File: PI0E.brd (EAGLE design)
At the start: 36 parts, among them T1 WE-LAN-10/100/1000-BASE-T,749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, X1 22-23-2021, X2 22-23-2021

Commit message: fixed missing RX line
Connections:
- net 3: now also T1.1
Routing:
- net 3: track 0.00 -> 23.4 mm, vias 0 -> 2
- net 1: track 21.2 -> 23.2 mm
- net 2: track 19.6 -> 21.3 mm
- net 6: track 17.5 -> 19.1 mm
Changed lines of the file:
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@@
 <layer number="17" name="Pads" color="2" fill="1" visible="yes" active="yes"/>
 <layer number="18" name="Vias" color="2" fill="1" visible="yes" active="yes"/>
-<layer number="19" name="Unrouted" color="6" fill="1" visible="no" active="yes"/>
+<layer number="19" name="Unrouted" color="6" fill="1" visible="yes" active="yes"/>
 <layer number="20" name="Dimension" color="15" fill="1" visible="no" active="yes"/>
 <layer number="21" name="tPlace" color="7" fill="1" visible="yes" active="yes"/>
@@
 <contactref element="U$4" pad="2"/>
 <contactref element="T1" pad="8"/>
-<wire x1="66.01" y1="29.761" x2="68.283" y2="29.761" width="0.4064" layer="1"/>
-<wire x1="68.283" y1="29.761" x2="69.596" y2="28.448" width="0.4064" layer="1"/>
-<wire x1="69.596" y1="28.448" x2="69.596" y2="20.828" width="0.4064" layer="1"/>
-<wire x1="69.596" y1="20.828" x2="67.056" y2="18.288" width="0.4064" layer="1"/>
-<wire x1="67.056" y1="18.288" x2="67.056" y2="14.079" width="0.4064" layer="1"/>
-<wire x1="67.056" y1="14.079" x2="67.052" y2="14.075" width="0.4064" layer="1"/>
+<wire x1="66.01" y1="29.761" x2="69.8832" y2="29.761" width="0.4064" layer="1"/>
+<wire x1="69.8832" y1="29.761" x2="70.5358" y2="29.1084" width="0.4064" layer="1"/>
+<wire x1="70.5358" y1="29.1084" x2="70.5358" y2="27.4193" width="0.4064" layer="1"/>
+<wire x1="70.5358" y1="27.4193" x2="69.8881" y2="26.7716" width="0.4064" layer="1"/>
+<wire x1="69.8881" y1="26.7716" x2="69.8881" y2="20.0406" width="0.4064" layer="1"/>
+<wire x1="69.8881" y1="20.0406" x2="67.0687" y2="17.2212" width="0.4064" layer="1"/>
+<wire x1="67.0687" y1="17.2212" x2="67.0687" y2="14.0917" width="0.4064" layer="1"/>
+<wire x1="67.0687" y1="14.0917" x2="67.052" y2="14.075" width="0.4064" layer="1"/>
 </signal>
 <signal name="6">
 <contactref element="U$4" pad="6"/>
 <contactref element="T1" pad="2"/>
-<wire x1="66.01" y1="25.708" x2="68.281" y2="25.689" width="0.4064" layer="1"/>
-<wire x1="74.672" y1="14.075" x2="74.608" y2="14.075" width="0.4064" layer="1"/>
-<via x="68.281" y="25.689" extent="1-16" drill="0.6096"/>
-<via x="72.789" y="18.128" extent="1-16" drill="0.6096"/>
-<wire x1="74.608" y1="14.075" x2="74.608" y2="15.308" width="0.4064" layer="1"/>
-<wire x1="74.608" y1="15.308" x2="72.898" y2="17.018" width="0.4064" layer="1"/>
-<wire x1="72.898" y1="17.018" x2="72.898" y2="18.019" width="0.4064" layer="1"/>
-<wire x1="72.898" y1="18.019" x2="72.789" y2="18.128" width="0.4064" layer="1"/>
-<wire x1="68.281" y1="25.689" x2="69.815" y2="25.689" width="0.4064" layer="16"/>
-<wire x1="69.815" y1="25.689" x2="72.644" y2="22.86" width="0.4064" layer="16"/>
-<wire x1="72.644" y1="22.86" x2="72.644" y2="18.273" width="0.4064" layer="16"/>
-<wire x1="72.644" y1="18.273" x2="72.789" y2="18.128" width="0.4064" layer="16"/>
+<wire x1="66.01" y1="25.708" x2="68.7356" y2="25.708" width="0.4064" layer="1"/>
+<wire x1="68.7356" y1="25.708" x2="68.7578" y2="25.7302" width="0.4064" layer="1"/>
+<via x="68.7578" y="25.7302" extent="1-16" drill="0.6"/>
+<wire x1="68.7578" y1="25.7302" x2="71.6661" y2="25.7302" width="0.4064" layer="16"/>
+<wire x1="71.6661" y1="25.7302" x2="71.7042" y2="25.6921" width="0.4064" layer="16"/>
+<via x="71.7042" y="25.6921" extent="1-16" drill="0.6"/>
+<wire x1="71.7042" y1="25.6921" x2="71.7042" y2="17.3609" width="0.4064" layer="1"/>
+<wire x1="71.7042" y1="17.3609" x2="73.4441" y2="15.621" width="0.4064" layer="1"/>
+<wire x1="73.4441" y1="15.621" x2="74.3458" y2="15.621" width="0.4064" layer="1"/>
+<wire x1="74.3458" y1="15.621" x2="74.7395" y2="15.2273" width="0.4064" layer="1"/>
+<wire x1="74.7395" y1="15.2273" x2="74.7395" y2="14.1425" width="0.4064" layer="1"/>
+<wire x1="74.7395" y1="14.1425" x2="74.672" y2="14.075" width="0.4064" layer="1"/>
 </signal>
 <signal name="+5V">
@@
 <contactref element="U$4" pad="1"/>
 <contactref element="T1" pad="7"/>
-<wire x1="66.01" y1="30.781" x2="68.533" y2="30.781" width="0.4064" layer="1"/>
-<wire x1="68.533" y1="30.781" x2="70.866" y2="28.448" width="0.4064" layer="1"/>
-<wire x1="70.866" y1="28.448" x2="70.866" y2="20.32" width="0.4064" layer="1"/>
-<wire x1="70.866" y1="20.32" x2="68.326" y2="17.78" width="0.4064" layer="1"/>
-<wire x1="68.326" y1="17.78" x2="68.326" y2="14.079" width="0.4064" layer="1"/>
-<wire x1="68.326" y1="14.079" x2="68.322" y2="14.075" width="0.4064" layer="1"/>
+<wire x1="68.322" y1="14.075" x2="68.322" y2="17.395" width="0.4064" layer="1"/>
+<wire x1="68.322" y1="17.395" x2="70.7517" y2="19.8247" width="0.4064" layer="1"/>
+<wire x1="70.7517" y1="19.8247" x2="70.7517" y2="26.3017" width="0.4064" layer="1"/>
+<wire x1="70.7517" y1="26.3017" x2="71.6661" y2="27.2923" width="0.4064" layer="1"/>
+<wire x1="71.6661" y1="27.2923" x2="71.6661" y2="29.8958" width="0.4064" layer="1"/>
+<wire x1="71.6661" y1="29.8958" x2="70.8025" y2="30.7594" width="0.4064" layer="1"/>
+<wire x1="70.8025" y1="30.7594" x2="66.0316" y2="30.7594" width="0.4064" layer="1"/>
+<wire x1="66.0316" y1="30.7594" x2="66.01" y2="30.781" width="0.4064" layer="1"/>
 </signal>
 <signal name="TX-">
@@
 <signal name="3">
 <contactref element="U$4" pad="3"/>
+<contactref element="T1" pad="1"/>
+<wire x1="75.942" y1="14.075" x2="75.942" y2="15.3329" width="0.4064" layer="1"/>
+<wire x1="75.942" y1="15.3329" x2="74.8792" y2="16.3957" width="0.4064" layer="1"/>
+<wire x1="74.8792" y1="16.3957" x2="73.8378" y2="16.3957" width="0.4064" layer="1"/>
+<wire x1="73.8378" y1="16.3957" x2="73.39965" y2="16.83385" width="0.4064" layer="1"/>
+<wire x1="73.39965" y1="16.83385" x2="73.0504" y2="17.1831" width="0.4064" layer="1"/>
+<wire x1="66.01" y1="28.741" x2="68.8331" y2="28.741" width="0.4064" layer="1"/>
+<wire x1="68.8331" y1="28.741" x2="68.8467" y2="28.7274" width="0.4064" layer="1"/>
+<via x="68.8467" y="28.7274" extent="1-16" drill="0.6"/>
+<wire x1="68.8467" y1="28.7274" x2="72.9234" y2="28.7274" width="0.4064" layer="16"/>
+<via x="72.9234" y="28.7274" extent="1-16" drill="0.6"/>
+<wire x1="72.9234" y1="28.7274" x2="72.9234" y2="17.3101" width="0.4064" layer="1"/>
+<wire x1="72.9234" y1="17.3101" x2="73.0504" y2="17.1831" width="0.4064" layer="1"/>
 </signal>
 <signal name="N$22">

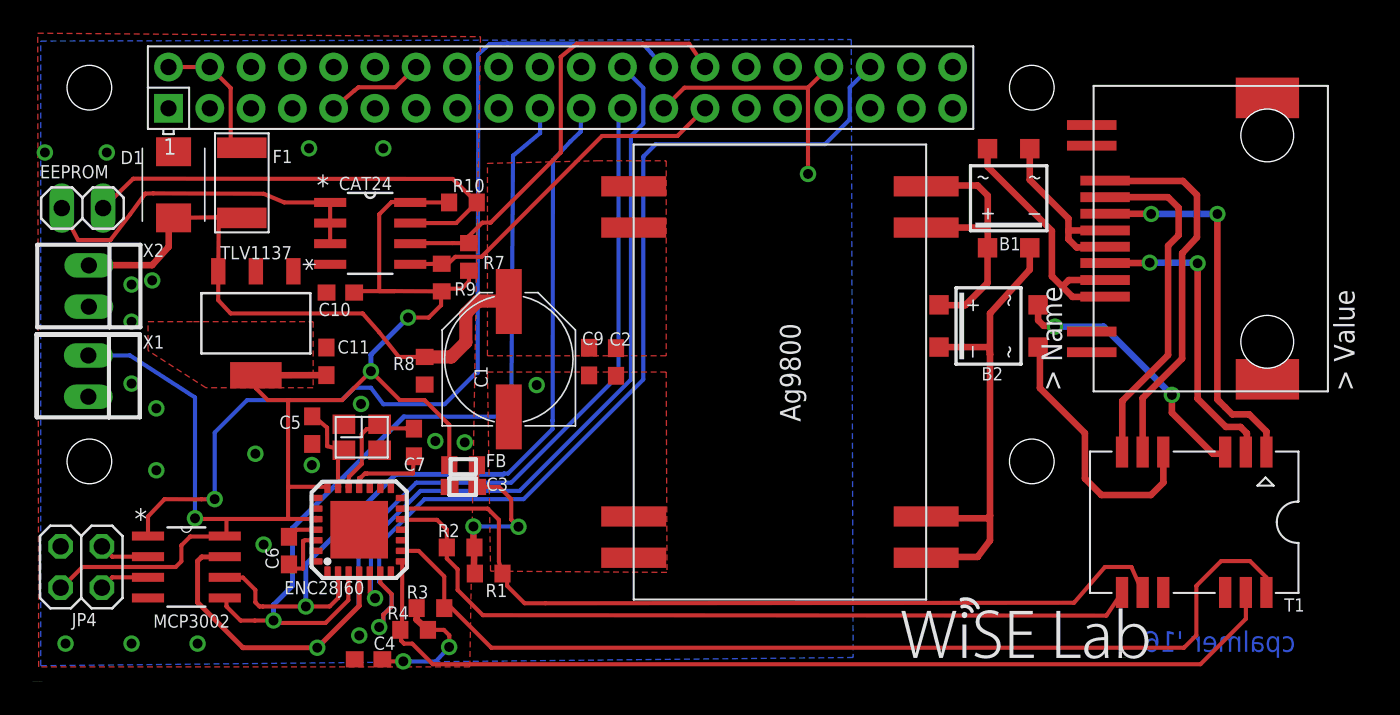
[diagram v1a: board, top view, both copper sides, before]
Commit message: fixed encj rx/tx power lines. and switch v+ v- pins into the poe module.
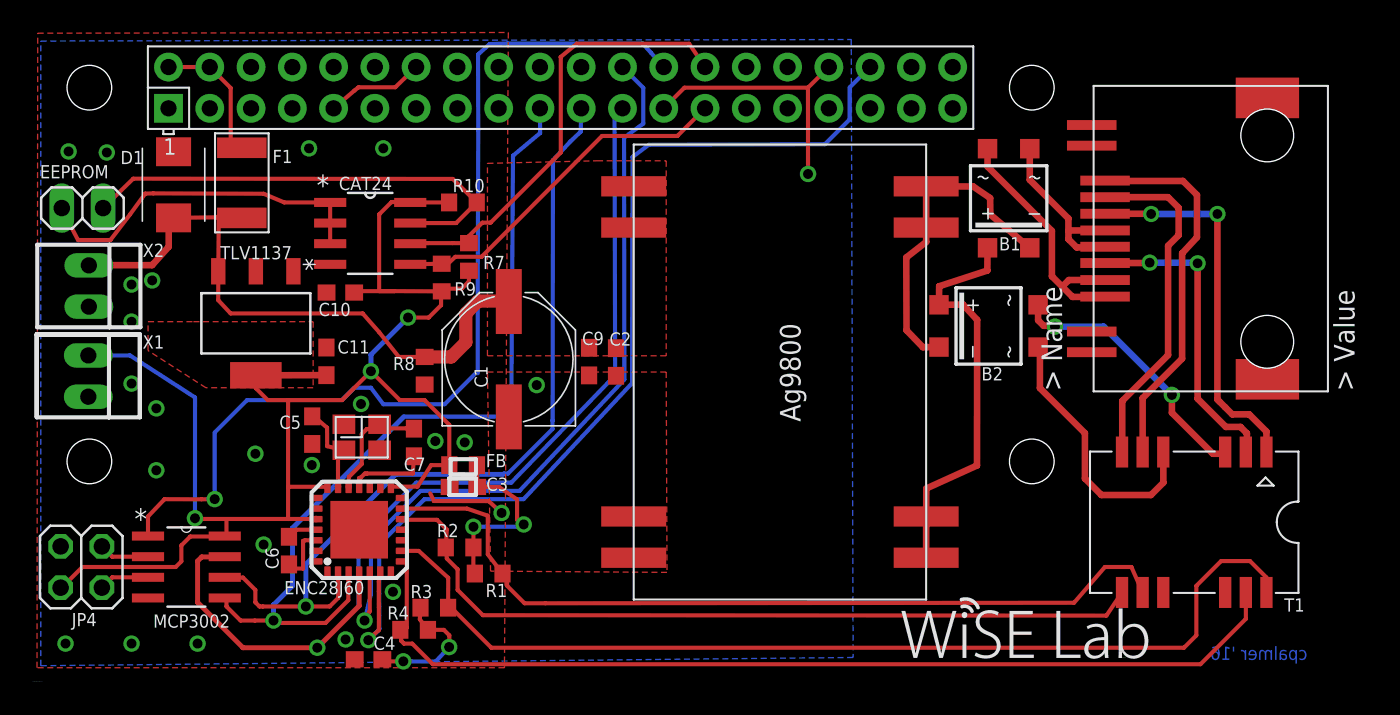
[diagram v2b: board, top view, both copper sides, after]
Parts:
- moved R3 0.24 mm to (24.7, 4.50)
- moved R2 0.06 mm to (26.3, 8.20)
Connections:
- net +3V3: now also ENC28J60.11, ENC28J60.15
- net GND: now also ENC28J60.14, ENC28J60.7
- net VIN+: now also B1.+, B2.+; no longer B1.-, B2.-
- net VIN-: now also B1.-, B2.-; no longer B1.+, B2.+
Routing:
- net VIN+: track 31.3 -> 25.8 mm
- net GND: track 53.2 -> 58.1 mm, vias 22 -> 24
- net +3V3: track 93.5 -> 97.9 mm
- net VIN-: track 17.0 -> 20.4 mm
- net !CS: track 45.5 -> 48.2 mm
- net !RESET: track 61.2 -> 62.3 mm
- net N$13: track 11.8 -> 12.4 mm

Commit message: update to bom. last air wires taken care of on board
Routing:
- net +3V3: track 97.9 -> 124.7 mm, vias 3 -> 5
- net GND: vias 24 -> 25
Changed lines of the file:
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@@
 <wire x1="28.0776" y1="11.0554" x2="24.7015" y2="11.0628" width="0.254" layer="1"/>
 <wire x1="24.7015" y1="11.0628" x2="24.4729" y2="11.5443" width="0.254" layer="1"/>
+<via x="31.7627" y="6.985" extent="1-16" drill="0.6096"/>
 </signal>
 <signal name="N$5">
@@
 <wire x1="20.755" y1="4.274" x2="20.4373" y2="3.7059" width="0.254" layer="1"/>
 <via x="20.4373" y="3.7059" extent="1-16" drill="0.6096"/>
-<wire x1="20.4373" y1="3.7059" x2="20.828" y2="5.334" width="0.254" layer="16"/>
-<wire x1="20.828" y1="5.334" x2="20.828" y2="8.636" width="0.254" layer="16"/>
+<wire x1="20.4373" y1="3.7059" x2="20.816" y2="4.301" width="0.254" layer="16"/>
+<wire x1="20.816" y1="4.301" x2="20.828" y2="8.636" width="0.254" layer="16"/>
 <wire x1="20.828" y1="8.636" x2="23.876" y2="11.684" width="0.254" layer="16"/>
 <wire x1="23.876" y1="11.684" x2="29.972" y2="11.684" width="0.254" layer="16"/>
@@
 <wire x1="3.073" y1="7.001" x2="8.815" y2="7.001" width="0.254" layer="1"/>
 <wire x1="8.815" y1="7.001" x2="9.162" y2="7.349" width="0.254" layer="1"/>
-<wire x1="9.162" y1="7.349" x2="9.162" y2="8.328" width="0.254" layer="1"/>
+<wire x1="9.162" y1="7.349" x2="9.162" y2="7.4422" width="0.254" layer="1"/>
+<wire x1="9.162" y1="7.4422" x2="9.162" y2="8.328" width="0.254" layer="1"/>
 <wire x1="9.162" y1="8.328" x2="9.711" y2="8.877" width="0.254" layer="1"/>
 <wire x1="24.13" y1="17.272" x2="22.606" y2="17.272" width="0.254" layer="1"/>
@@
 <wire x1="23.694" y1="11.948" x2="24.532" y2="13.271" width="0.254" layer="1"/>
 <wire x1="24.532" y1="13.271" x2="25.652" y2="13.269" width="0.254" layer="1"/>
-<wire x1="22.055" y1="11.945" x2="22.755" y2="9.295" width="0" layer="19" extent="1-1"/>
+<wire x1="22.755" y1="9.295" x2="23.8252" y2="9.3091" width="0.254" layer="1"/>
+<wire x1="23.8252" y1="9.3091" x2="23.9395" y2="8.8773" width="0.254" layer="1"/>
+<wire x1="23.9395" y1="8.8773" x2="23.9141" y2="3.556" width="0.254" layer="16"/>
+<wire x1="23.9141" y1="3.556" x2="21.2591" y2="1.1807" width="0.254" layer="16"/>
+<via x="14.8456" y="1.1691" extent="1-16" drill="0.6096"/>
+<wire x1="14.8456" y1="1.1691" x2="13.83645" y2="1.169175" width="0.254" layer="1"/>
+<wire x1="13.83645" y1="1.169175" x2="12.279" y2="1.168" width="0.254" layer="1"/>
+<wire x1="12.279" y1="1.168" x2="9.167" y2="4.7498" width="0.254" layer="1"/>
+<wire x1="9.167" y1="4.7498" x2="9.162" y2="7.4422" width="0.254" layer="1"/>
+<via x="23.9395" y="8.8773" extent="1-16" drill="0.6096"/>
+<wire x1="21.2591" y1="1.1807" x2="14.8456" y2="1.1691" width="0.254" layer="16"/>
 </signal>
 <signal name="N$18">
@@
 <wire x1="21.3113" y1="6.1091" x2="21.3113" y2="5.5067" width="0.254" layer="1"/>
 <wire x1="21.3113" y1="5.5067" x2="21.314" y2="4.7227" width="0.254" layer="1"/>
-<wire x1="21.314" y1="4.7227" x2="21.3134" y2="4.5281" width="0.254" layer="1"/>
-<wire x1="21.3134" y1="4.5281" x2="21.319" y2="3.628" width="0.254" layer="1"/>
-<wire x1="21.319" y1="3.628" x2="21.312" y2="3.107" width="0.254" layer="1"/>
-<wire x1="21.312" y1="3.107" x2="20.977" y2="2.821" width="0.254" layer="1"/>
-<wire x1="20.977" y1="2.821" x2="20.6669" y2="2.4987" width="0.254" layer="1"/>
-<via x="20.6669" y="2.4987" extent="1-16" drill="0.6096"/>
-<wire x1="20.6669" y1="2.4987" x2="21.284" y2="3.091" width="0.254" layer="16"/>
+<wire x1="21.314" y1="4.7227" x2="21.3134" y2="4.5161" width="0.254" layer="1"/>
+<wire x1="21.3134" y1="4.5161" x2="21.319" y2="3.616" width="0.254" layer="1"/>
+<wire x1="21.319" y1="3.616" x2="21.324" y2="3.095" width="0.254" layer="1"/>
+<wire x1="21.324" y1="3.095" x2="20.965" y2="2.882" width="0.254" layer="1"/>
+<wire x1="20.965" y1="2.882" x2="20.6059" y2="2.6317" width="0.254" layer="1"/>
+<via x="20.6059" y="2.6317" extent="1-16" drill="0.6096"/>
+<wire x1="20.6059" y1="2.6317" x2="21.284" y2="3.091" width="0.254" layer="16"/>
 <wire x1="21.284" y1="3.091" x2="21.346" y2="3.194" width="0.254" layer="16"/>
 <wire x1="21.346" y1="3.194" x2="21.339" y2="4.008" width="0.254" layer="16"/>
@@
 <wire x1="20.105" y1="6.645" x2="20.105" y2="4.611" width="0.3048" layer="1"/>
 <wire x1="20.105" y1="4.611" x2="17.526" y2="2.032" width="0.3048" layer="1"/>
-<wire x1="17.526" y1="2.032" x2="12.954" y2="2.032" width="0.3048" layer="1"/>
-<wire x1="12.954" y1="2.032" x2="10.16" y2="4.826" width="0.3048" layer="1"/>
-<wire x1="10.16" y1="4.826" x2="10.16" y2="7.366" width="0.3048" layer="1"/>
-<wire x1="10.16" y1="7.366" x2="10.414" y2="7.62" width="0.3048" layer="1"/>
-<wire x1="10.414" y1="7.62" x2="11.8182" y2="7.62" width="0.3048" layer="1"/>
+<wire x1="17.526" y1="2.032" x2="12.954" y2="2.032" width="0.254" layer="1"/>
+<wire x1="12.954" y1="2.032" x2="10.16" y2="4.826" width="0.254" layer="1"/>
+<wire x1="10.16" y1="4.826" x2="10.16" y2="7.366" width="0.254" layer="1"/>
+<wire x1="10.16" y1="7.366" x2="10.414" y2="7.62" width="0.254" layer="1"/>
+<wire x1="10.414" y1="7.62" x2="11.8182" y2="7.62" width="0.254" layer="1"/>
 <wire x1="11.8182" y1="7.62" x2="11.8332" y2="7.635" width="0.3048" layer="1"/>
 <via x="17.526" y="2.032" extent="1-16" drill="0.6096"/>

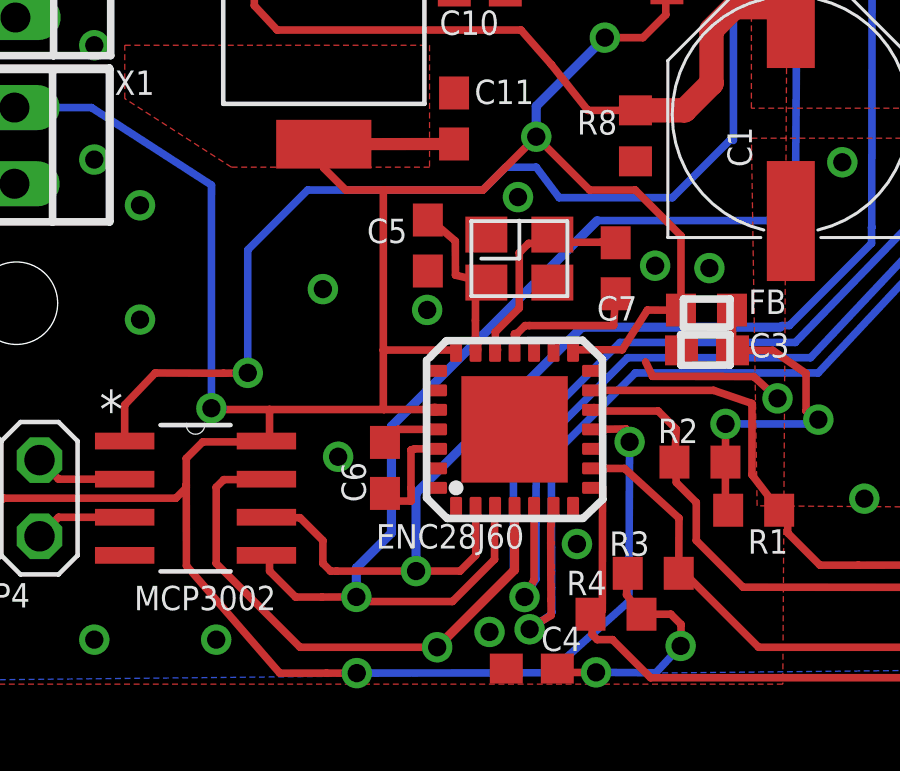
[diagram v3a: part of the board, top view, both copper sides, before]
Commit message: lengthened qfn pins, fixed drc errors
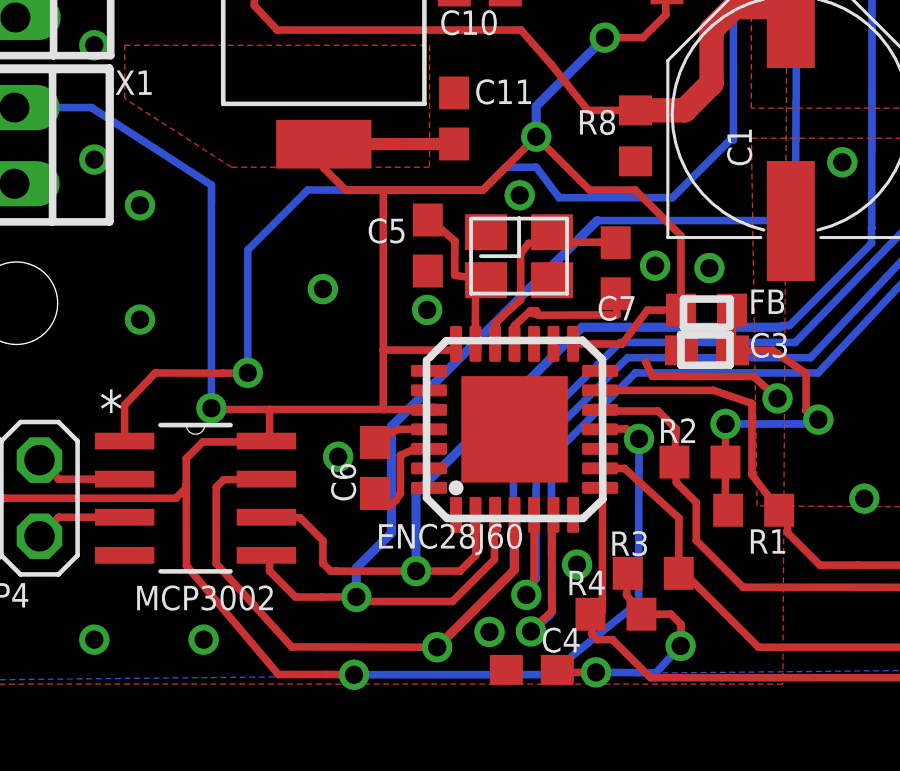
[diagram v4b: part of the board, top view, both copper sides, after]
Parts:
- moved C6 0.34 mm to (15.4, 8.01)
- moved OSC 0.08 mm to (20.3, 15.1)
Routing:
- net GND: track 58.1 -> 59.0 mm
